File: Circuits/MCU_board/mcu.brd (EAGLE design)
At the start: 80 x 70 mm, 72 parts, among them IC1 RP111N331B-TR-FE, IC2 FT230XS, U1 TCA9548APWR, U2 USBLC6-2P6, U4 LSM9DS1, U5 STM32L452RECT6

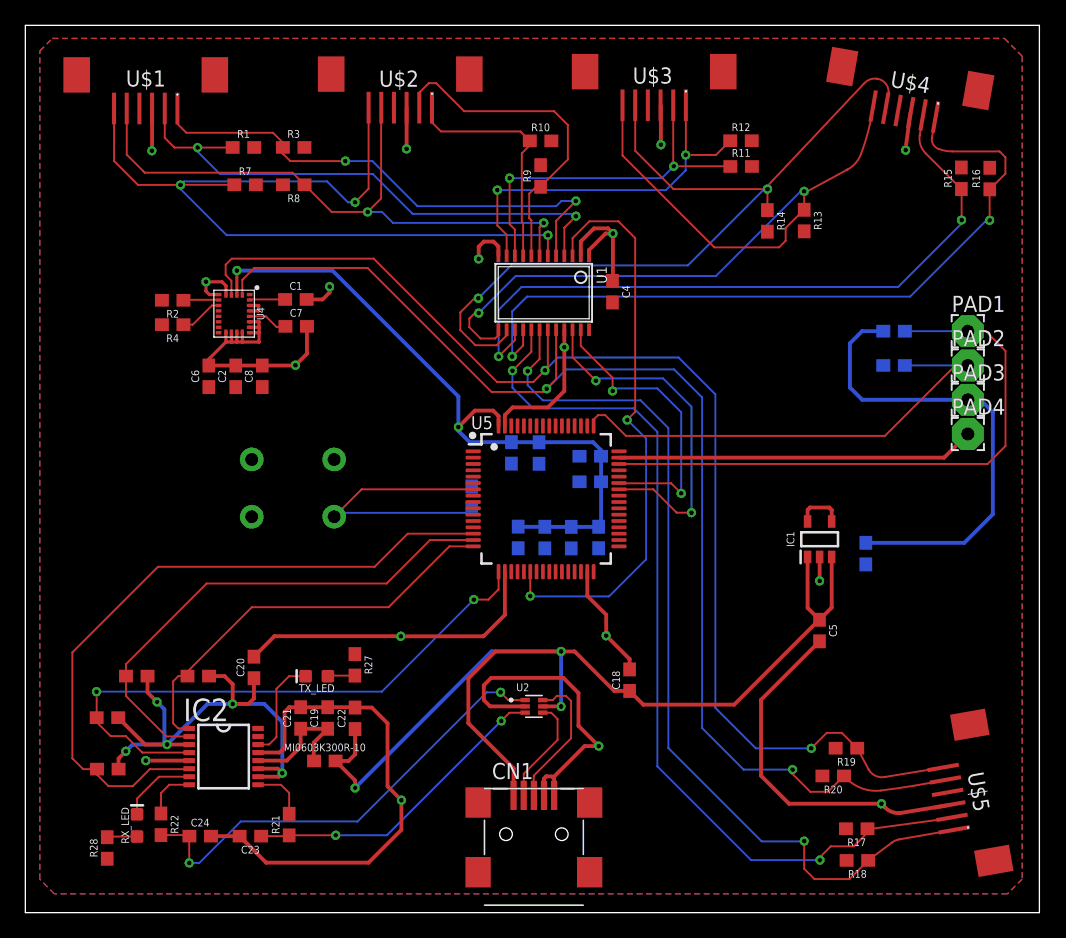
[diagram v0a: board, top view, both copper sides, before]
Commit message: Added thermal vias (not really sure if necessary)
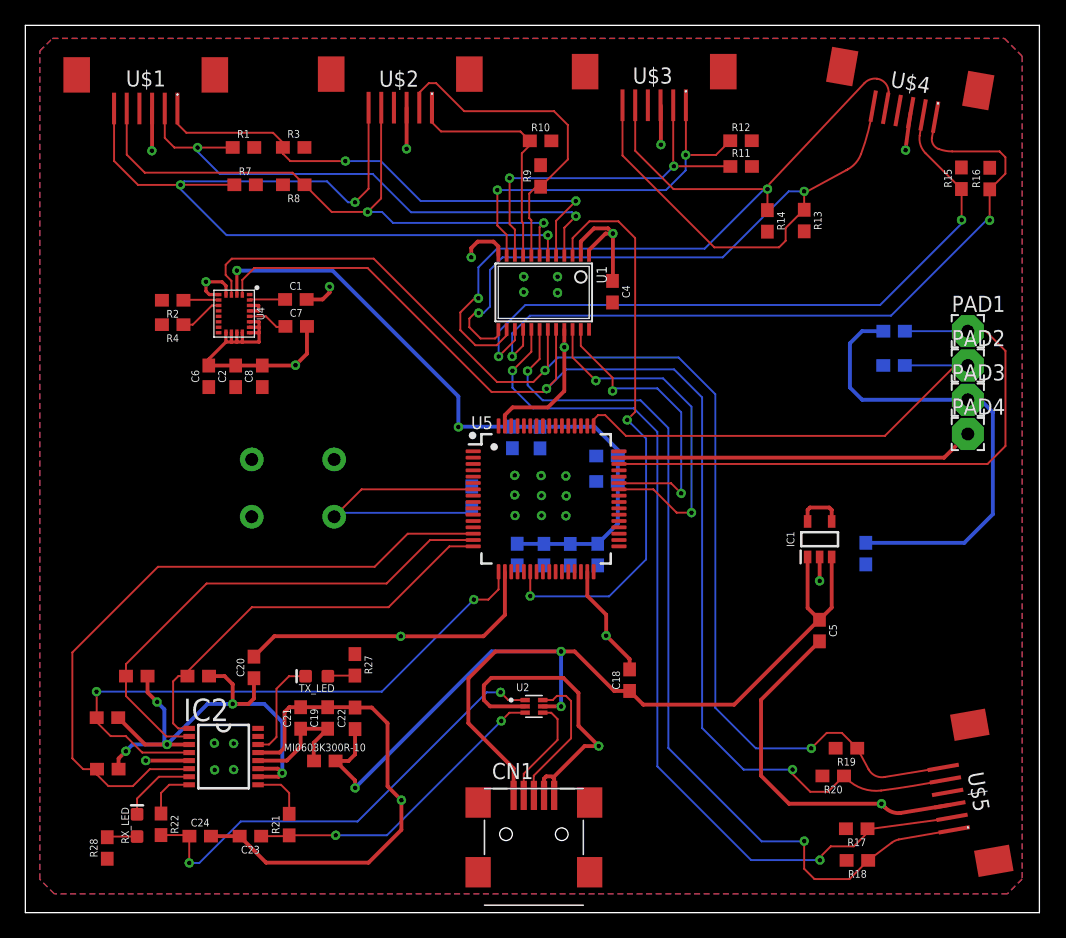
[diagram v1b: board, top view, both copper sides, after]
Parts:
- moved C14 1.35 mm to (45.2, 38.2)
- moved C13 1.35 mm to (43.0, 38.2)
- moved C15 1.35 mm to (38.8, 38.3)
- moved C16 1.35 mm to (40.9, 38.2)
- moved C11 1.32 mm to (45.9, 44.0)
- moved C12 1.32 mm to (45.9, 46.0)
- moved C10 1.22 mm to (38.4, 47.5)
- moved C9 1.22 mm to (40.6, 47.5)
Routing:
- net SDA4: track 68.4 -> 70.1 mm
- net VDD: track 98.6 -> 97.1 mm
- net SCL4: track 66.7 -> 68.1 mm
- net SDA5: track 55.5 -> 54.5 mm
- net SCL5: track 60.3 -> 59.3 mm

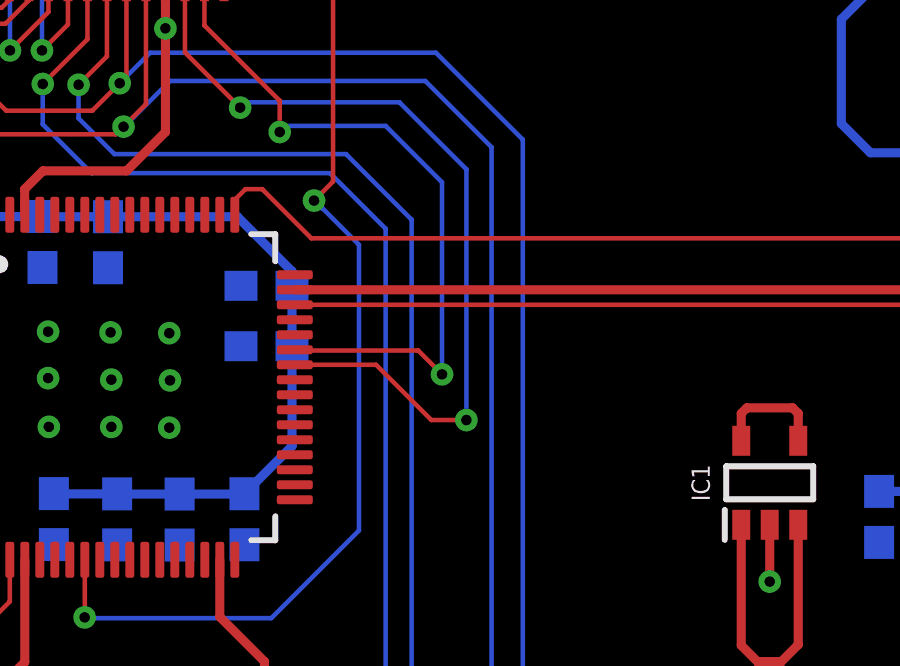
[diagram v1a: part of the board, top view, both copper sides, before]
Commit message: Add pullups for MCU I2C lines
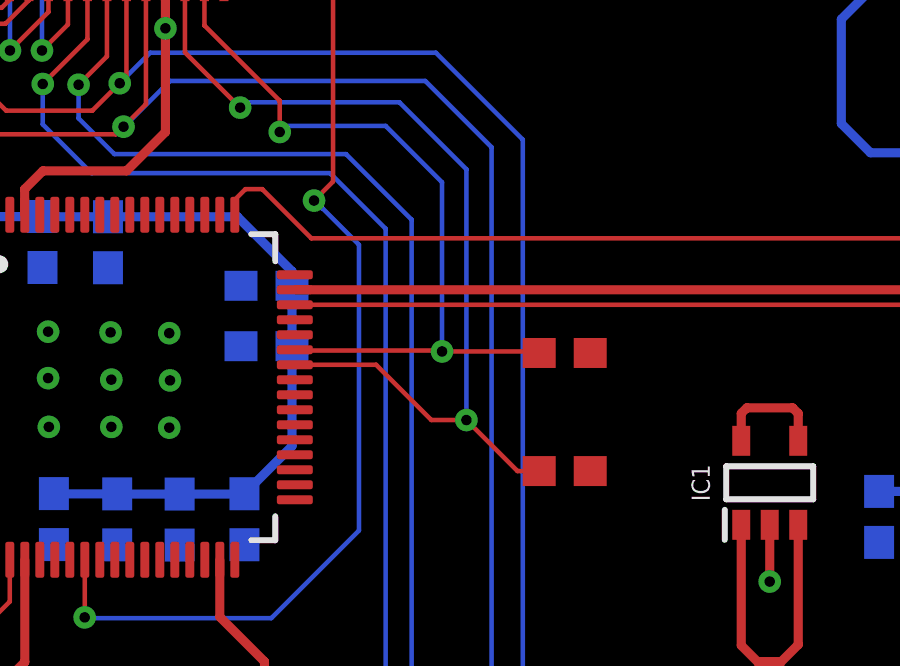
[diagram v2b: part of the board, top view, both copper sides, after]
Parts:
- added R29, R30: 10k, SparkFun-Resistors:0603
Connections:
- net I2C_SCLK: now also R29.1
- net I2C_SDA: now also R30.1
- net VDD: now also R29.2, R30.2
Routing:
- net I2C_SCLK: track 28.2 -> 31.3 mm
- net I2C_SDA: track 23.8 -> 26.0 mm
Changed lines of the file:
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@@
 <?xml version="1.0" encoding="utf-8"?>
 <!DOCTYPE eagle SYSTEM "eagle.dtd">
-<eagle version="9.4.2">
+<eagle version="9.3.2">
 <drawing>
 <settings>
-<setting alwaysvectorfont="yes"/>
+<setting alwaysvectorfont="no"/>
 <setting verticaltext="up"/>
 </settings>
-<grid distance="1" unitdist="mil" unit="mil" style="lines" multiple="1" display="yes" altdistance="5" altunitdist="mil" altunit="mil"/>
+<grid distance="10" unitdist="mil" unit="mil" style="lines" multiple="1" display="yes" altdistance="5" altunitdist="mil" altunit="mil"/>
 <layers>
 <layer number="1" name="Top" color="4" fill="1" visible="yes" active="yes"/>
@@
 <attribute name="MEM" value="" x="61.4022" y="35.0262" size="1.778" layer="27" display="off"/>
 <attribute name="MFPN" value="STM32L476RCT6" x="61.4022" y="35.0262" size="1.778" layer="27" display="off"/>
+<attribute name="NAME" x="41.0822" y="44.5462" size="0.8128" layer="151" ratio="10" align="center"/>
 <attribute name="NAME" x="36.8822" y="48.1462" size="1.016" layer="25" font="vector" ratio="18" align="bottom-right"/>
-<attribute name="NAME" x="41.0822" y="44.5462" size="0.8128" layer="151" ratio="10" align="center"/>
 <attribute name="PARTNO" value="" x="61.4022" y="35.0262" size="1.778" layer="27" display="off"/>
 <attribute name="STATUS" value="" x="61.4022" y="35.0262" size="1.778" layer="27" display="off"/>
@@
 <attribute name="PROD_ID" value="RES-00824" x="8.789" y="28.6616" size="1.778" layer="27" display="off"/>
 <attribute name="VALUE" x="8.789" y="27.8996" size="0.6096" layer="27" font="vector" ratio="20" align="top-center"/>
+</element>
+<element name="R29" library="SparkFun-Resistors" package="0603" value="10k" x="55.8292" y="39.8526" smashed="yes">
+<attribute name="PROD_ID" value="RES-00824" x="55.8292" y="39.8526" size="1.778" layer="27" display="off"/>
+<attribute name="VALUE" x="55.8292" y="39.0906" size="0.6096" layer="27" font="vector" ratio="20" align="top-center"/>
+</element>
+<element name="R30" library="SparkFun-Resistors" package="0603" value="10k" x="55.8292" y="43.7896" smashed="yes">
+<attribute name="PROD_ID" value="RES-00824" x="55.8292" y="43.7896" size="1.778" layer="27" display="off"/>
+<attribute name="VALUE" x="55.8292" y="43.0276" size="0.6096" layer="27" font="vector" ratio="20" align="top-center"/>
 </element>
 </elements>
@@
 <wire x1="63.613" y1="41.7716" x2="63.613" y2="40.8612" width="0.3048" layer="1"/>
 <wire x1="63.4238" y1="41.9608" x2="63.613" y2="41.7716" width="0.3048" layer="1"/>
+<contactref element="R29" pad="2"/>
+<contactref element="R30" pad="2"/>
 </signal>
 <signal name="USB_D-">
@@
 <wire x1="43.82" y1="54.7066" x2="46.3296" y2="52.197" width="0.1524" layer="1"/>
 <wire x1="46.3296" y1="52.197" x2="46.3296" y2="51.1556" width="0.1524" layer="1"/>
-<via x="51.7398" y="43.0784" extent="1-16" drill="0.35"/>
-<wire x1="50.9474" y1="43.8708" x2="46.8576" y2="43.8708" width="0.1524" layer="1"/>
+<via x="51.7398" y="43.8404" extent="1-16" drill="0.35"/>
 <wire x1="46.8322" y1="43.8962" x2="46.8576" y2="43.8708" width="0.1524" layer="1"/>
-<wire x1="50.9474" y1="43.8708" x2="51.7398" y2="43.0784" width="0.1524" layer="1"/>
 <wire x1="51.7398" y1="49.4792" x2="49.8602" y2="51.3588" width="0.1524" layer="16"/>
 <wire x1="49.8602" y1="51.3588" x2="46.5328" y2="51.3588" width="0.1524" layer="16"/>
 <wire x1="46.3296" y1="51.1556" x2="46.5328" y2="51.3588" width="0.1524" layer="16"/>
-<wire x1="51.7398" y1="49.4792" x2="51.7398" y2="43.0784" width="0.1524" layer="16"/>
+<contactref element="R30" pad="1"/>
+<wire x1="51.7094" y1="43.8708" x2="51.7398" y2="43.8404" width="0.1524" layer="1"/>
+<wire x1="46.8576" y1="43.8708" x2="51.7094" y2="43.8708" width="0.1524" layer="1"/>
+<wire x1="51.7398" y1="43.8404" x2="51.7398" y2="49.4792" width="0.1524" layer="16"/>
+<wire x1="51.7398" y1="43.8404" x2="54.9284" y2="43.8404" width="0.1524" layer="1"/>
+<wire x1="54.9284" y1="43.8404" x2="54.9792" y2="43.7896" width="0.1524" layer="1"/>
 </signal>
 <signal name="I2C_SCLK">
@@
 <wire x1="50.3174" y1="52.1462" x2="52.5526" y2="49.911" width="0.1524" layer="16"/>
 <wire x1="52.5526" y1="49.911" x2="52.5526" y2="41.5544" width="0.1524" layer="16"/>
+<contactref element="R29" pad="1"/>
+<wire x1="52.5526" y1="41.5544" x2="54.2544" y2="39.8526" width="0.1524" layer="1"/>
+<wire x1="54.2544" y1="39.8526" x2="54.9792" y2="39.8526" width="0.1524" layer="1"/>
 </signal>
 <signal name="D+">

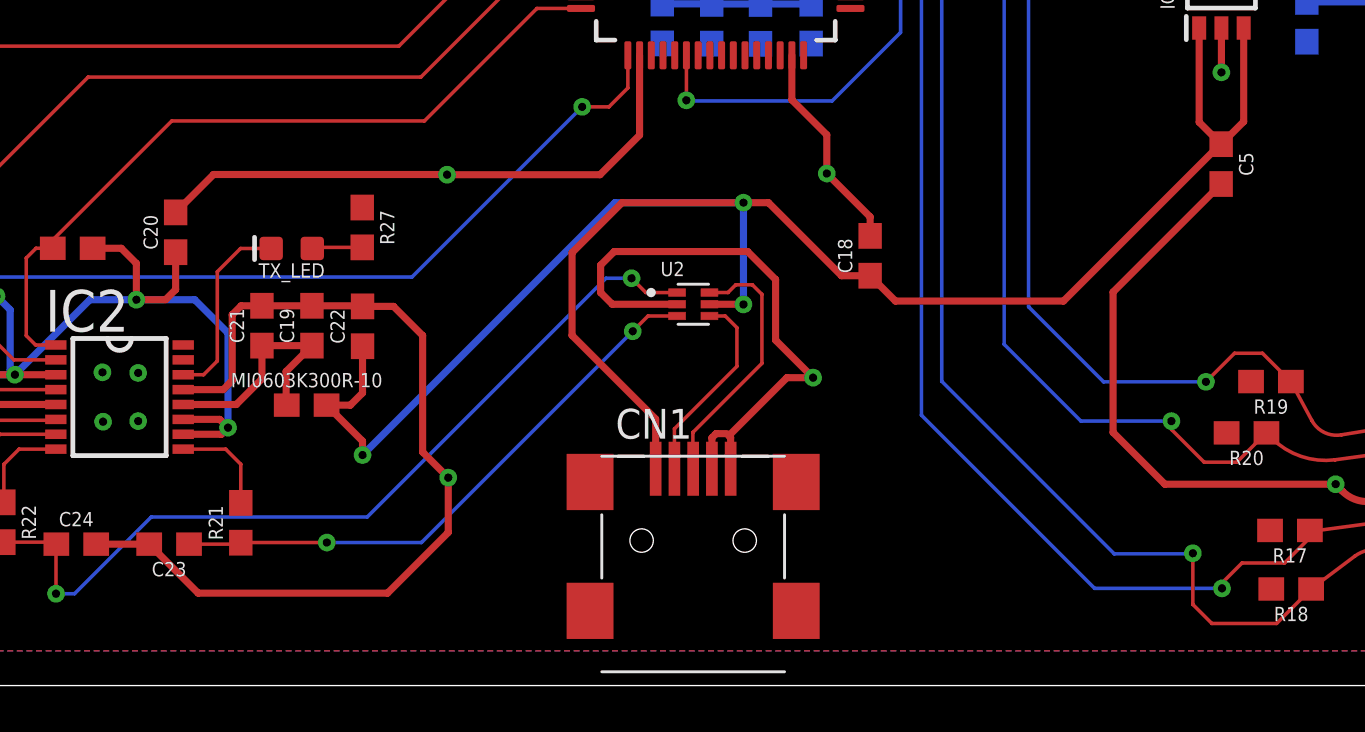
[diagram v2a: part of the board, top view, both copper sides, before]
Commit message: Change diode routing
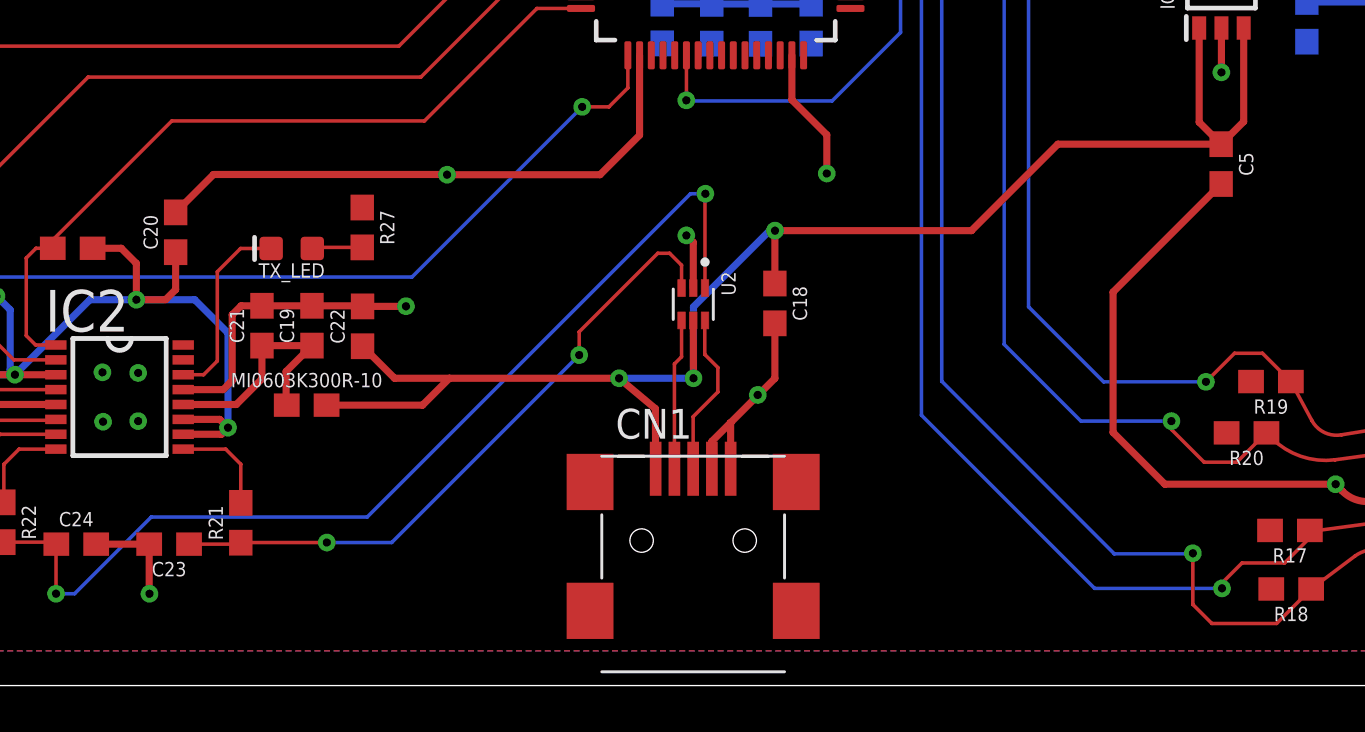
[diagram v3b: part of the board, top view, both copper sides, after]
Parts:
- moved C18 4.54 mm to (43.6, 26.3), turned to 270 degrees
- turned U2 to 270 degrees
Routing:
- net GND: track 229.8 -> 189.8 mm, vias 17 -> 19
- net VBUS: track 87.5 -> 68.9 mm
- net USB_D+: track 36.7 -> 43.2 mm
- net D+: track 11.2 -> 7.00 mm
- net USB_D-: track 24.9 -> 27.9 mm
- net D-: track 8.51 -> 6.46 mm

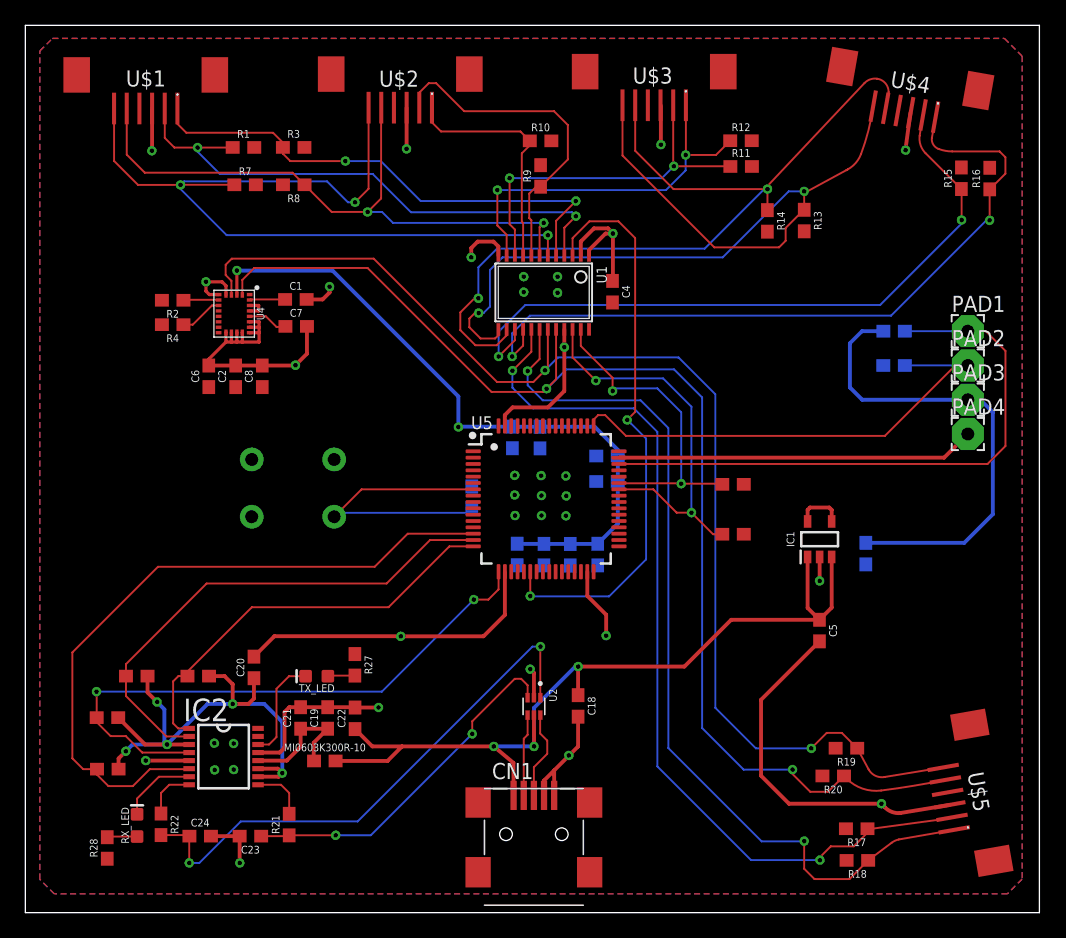
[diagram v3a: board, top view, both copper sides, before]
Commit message: Changed routing on FTDI, Added Testpads for each plane, Changed some connector traces
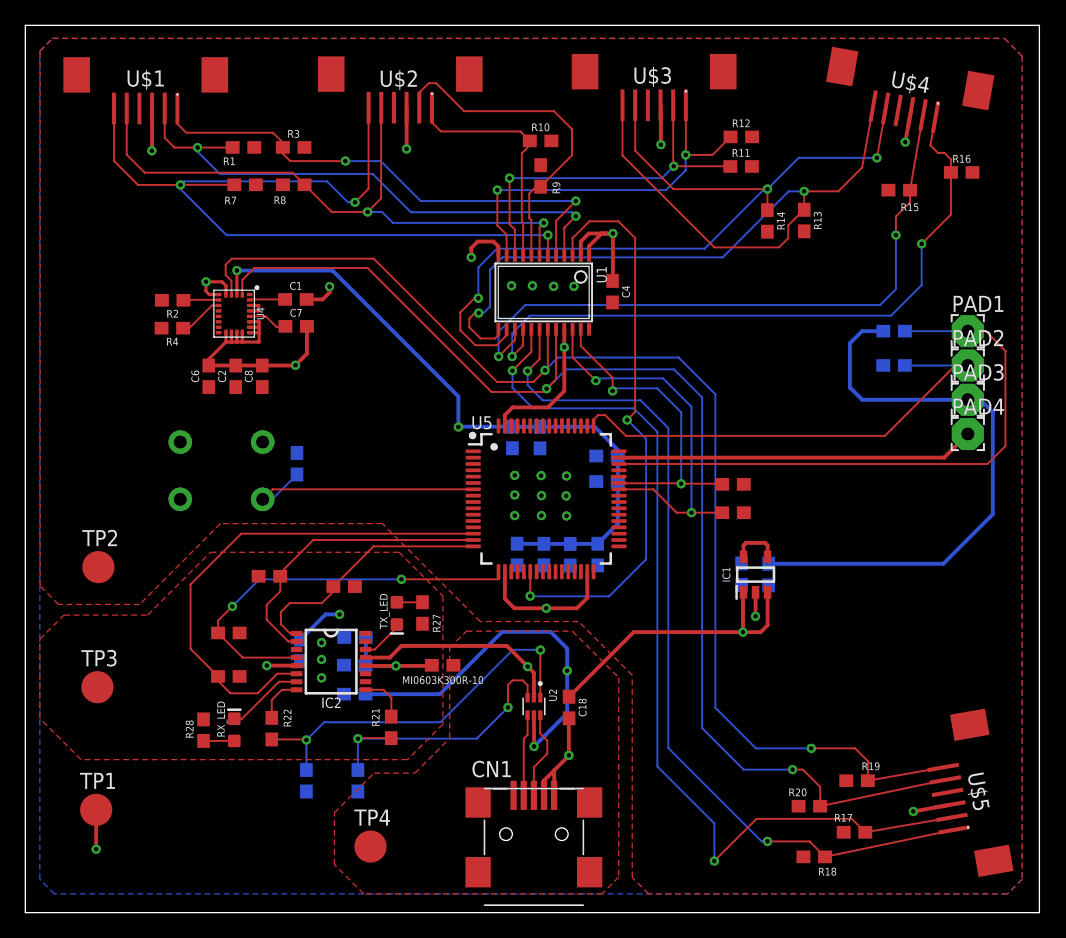
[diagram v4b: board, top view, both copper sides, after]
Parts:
- added TP1, TP2, TP3, TP4: TPB2,54, testpad:B2,54
- moved C17 14.0 mm to (21.4, 45.4)
- moved R23 13.5 mm to (25.1, 35.7)
- moved R26 13.1 mm to (19.3, 36.5), turned to 180 degrees
- moved R25 12.0 mm to (16.1, 28.6)
- moved R28 12.0 mm to (14.1, 24.4), turned to 270 degrees
- moved MI0603K300R-10 12.0 mm to (32.9, 29.5)
- moved R24 11.7 mm to (16.1, 32.1)
- moved R22 11.5 mm to (19.4, 24.5)
- moved IC2 11.3 mm to (24.1, 29.8)
- moved R21 11.1 mm to (28.9, 24.6)
- moved RX_LED 10.8 mm to (16.5, 24.4)
- moved C23 9.54 mm to (26.2, 20.4), flipped to the bottom, turned to 270 degrees
- moved C24 9.45 mm to (22.2, 20.4), flipped to the bottom, turned to 270 degrees
- moved TX_LED 8.03 mm to (29.3, 33.6), turned to 270 degrees
- moved C3 7.85 mm to (58.6, 36.7)
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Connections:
- net GND: now also TP1.TP
- net VBUS: now also TP4.TP
- net VCCIO: now also R27.1, R28.1, TP3.TP
- net VDD: now also TP2.TP; no longer R27.1, R28.1
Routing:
- net GND: track 189.8 -> 143.2 mm, vias 19 -> 17
- net VCCIO: track 43.9 -> 3.92 mm, vias 5 -> 1
- net RTS: track 40.3 -> 23.5 mm
- net RXD: track 47.2 -> 32.1 mm
- net CTS: track 54.8 -> 39.7 mm
- net TXD: track 33.0 -> 20.1 mm
- net USB_D+: track 43.2 -> 30.3 mm
- net VBUS: track 68.9 -> 57.3 mm
- net VDD: track 97.1 -> 105.4 mm
- net SCL5: track 59.3 -> 53.4 mm
- net USB_D-: track 27.9 -> 22.6 mm
- net CBUS1: track 8.22 -> 3.42 mm
- net SCL6: track 71.9 -> 68.9 mm
- net SDA5: track 54.5 -> 51.7 mm
- net NRST: track 23.0 -> 20.5 mm
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- added copper zone on layer 1, net VBUS
- added copper zone on layer 1, net VCCIO
